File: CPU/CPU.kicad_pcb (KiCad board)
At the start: 4 copper layers, 364 x 203 mm, 347 parts, among them J1 Conn_02x36_Top_Bottom, P2 Conn_02x13_Top_Bottom, P3 Conn_02x13_Top_Bottom, P4 IDC-16, P5 Conn_02x25_Counter_Clockwise, P6 Conn_02x25_Counter_Clockwise, P7 Conn_02x07_Counter_Clockwise, P8 Conn_02x08_Odd_Even

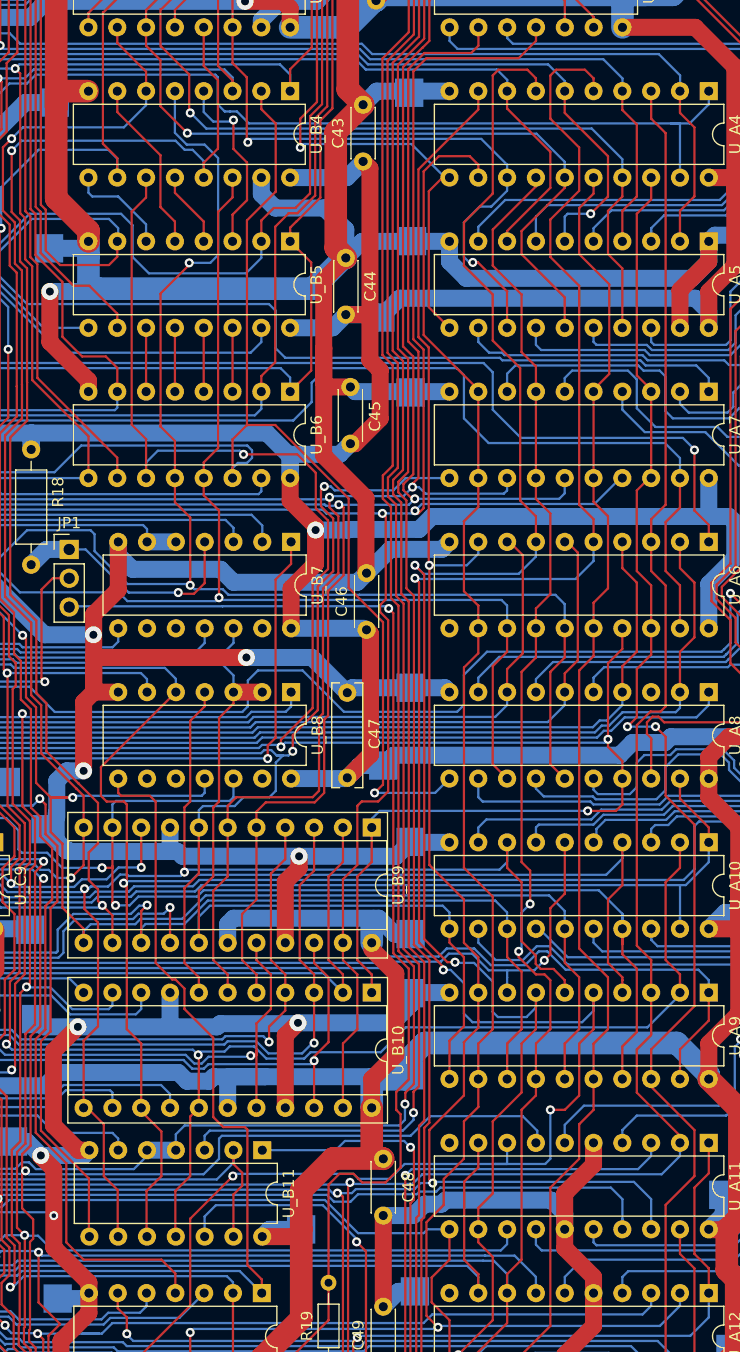
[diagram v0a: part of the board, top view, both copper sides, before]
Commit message: CPU: Erratum E003
Found and fixed a missing connection
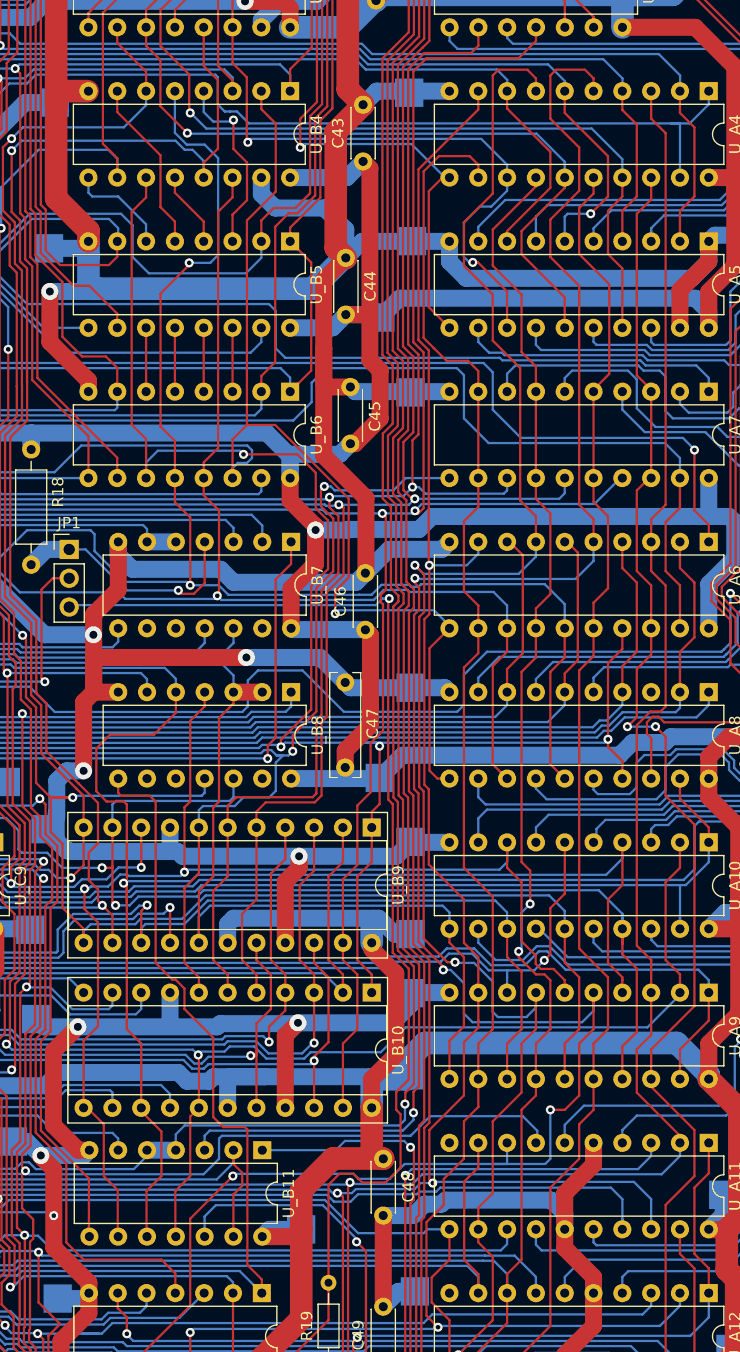
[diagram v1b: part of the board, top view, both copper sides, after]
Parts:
- moved +5V 1.13 mm to (340.6, 129.5)
- moved C47 0.92 mm to (337.5, 128.6)
- moved C46 0.10 mm to (339.3, 116.4)
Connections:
- U_A6 pad 11: unconnected-(U_A6-Pad11) -> Address.A_{8}
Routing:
- net Address.A_{11}: track 194.1 -> 177.2 mm
- net /PTR.Q_{5}: track 157.0 -> 159.6 mm
- net Address.A_{8}: track 164.5 -> 166.9 mm
- net DataP.D_{7}: track 709.5 -> 710.8 mm
- net Address.A_{12}: track 214.4 -> 213.2 mm
- net Net-(JP1-Pad3): track 114.9 -> 116.1 mm
- net Address.A_{10}: track 147.0 -> 148.0 mm
- net Address.A_{9}: track 121.5 -> 122.1 mm
- net DataP.D_{2}: track 630.2 -> 630.7 mm

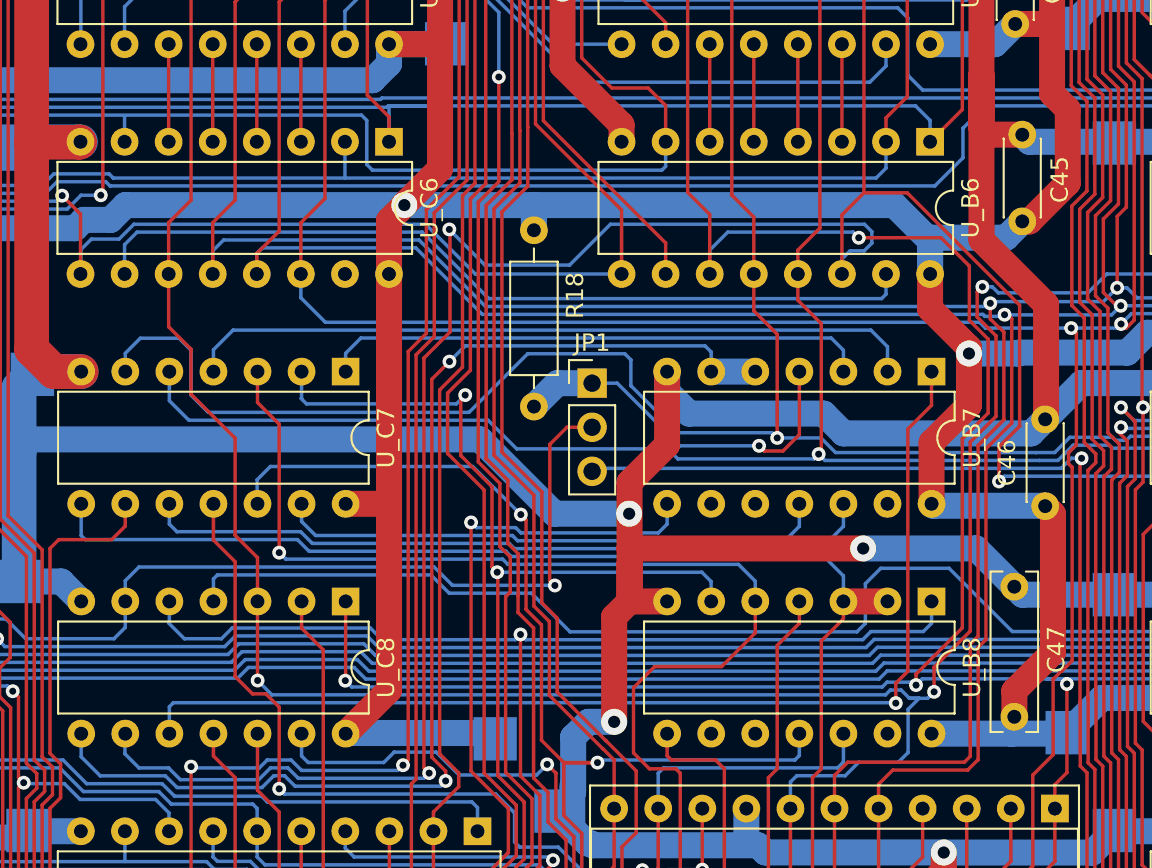
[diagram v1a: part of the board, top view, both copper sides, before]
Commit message: CPU: Straighten more ugly routing
Minus one via and loop around it
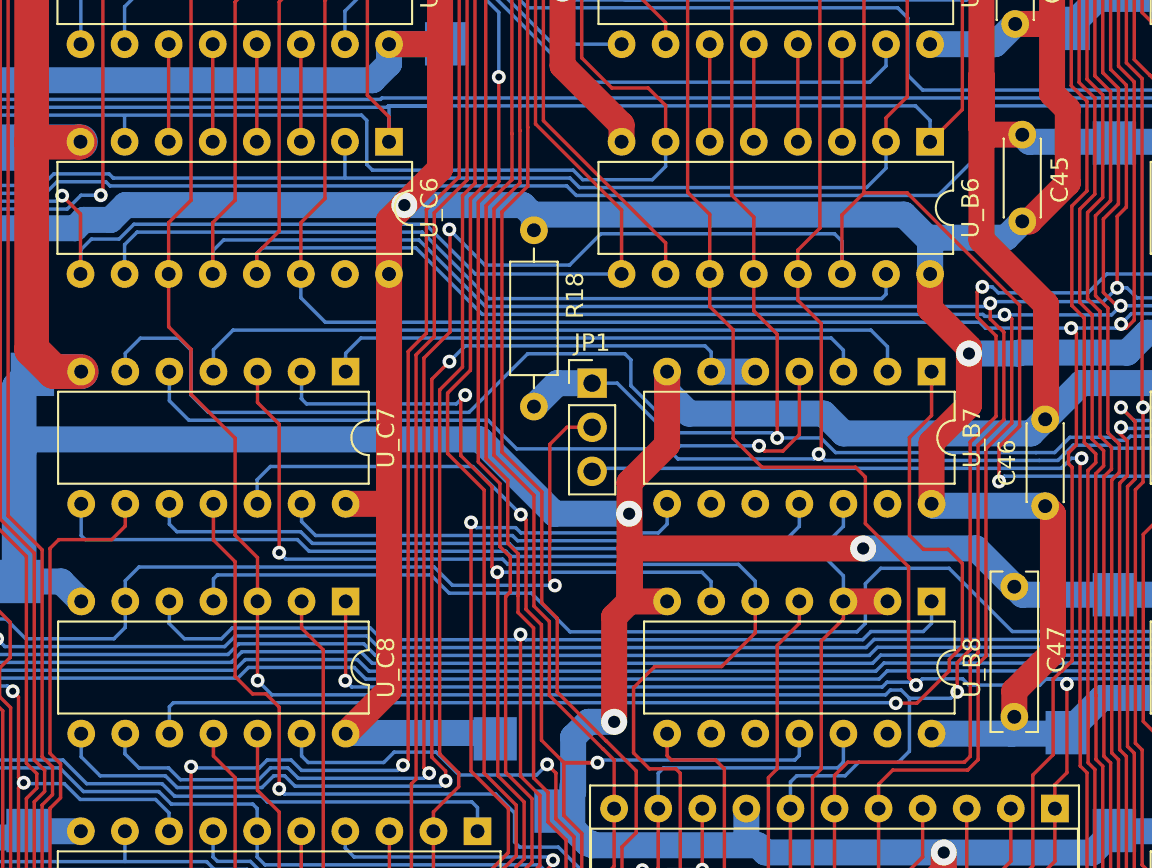
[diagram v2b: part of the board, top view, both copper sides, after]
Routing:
- net Address.A_{11}: track 177.2 -> 165.4 mm, vias 5 -> 4
- net Net-(U_B7-Pad1): track 63.5 -> 67.6 mm
- net Address.A_{8}: track 166.9 -> 163.2 mm
- net +5V: track 4533.4 -> 4532.3 mm
- net /~{AddrMToData}: track 179.0 -> 179.8 mm

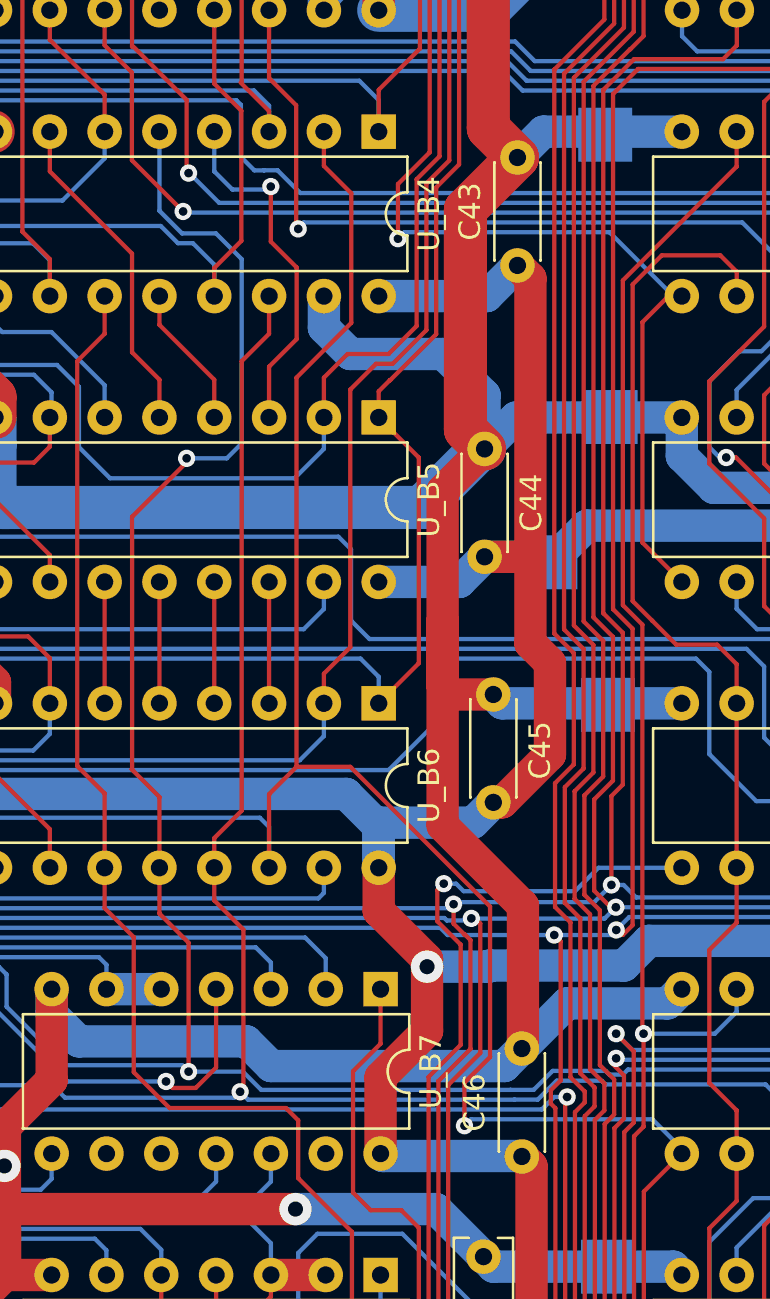
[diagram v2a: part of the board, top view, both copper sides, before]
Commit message: CPU: More clean up
Noticed some free space, left after the last optimization, and used it to move
tracks further away from pads
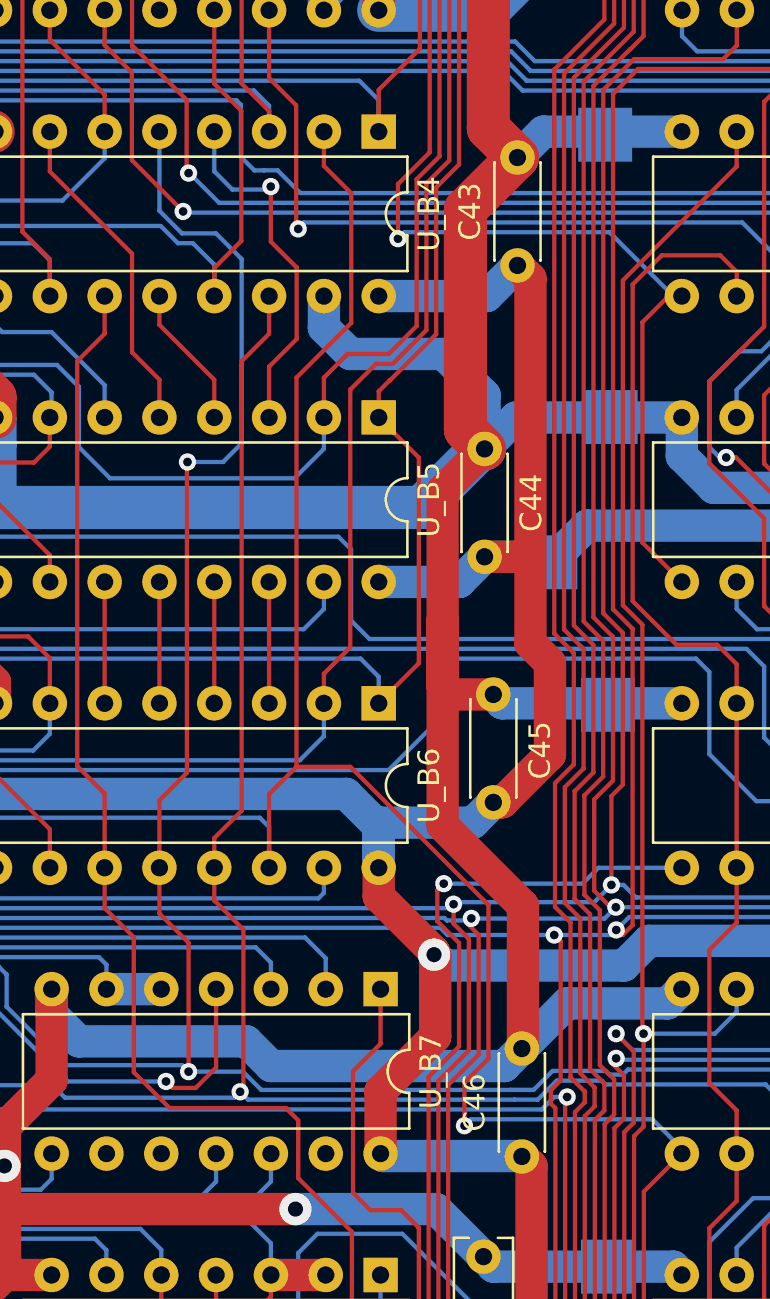
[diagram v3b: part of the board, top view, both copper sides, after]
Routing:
- net Address.A_{10}: track 148.0 -> 146.8 mm
